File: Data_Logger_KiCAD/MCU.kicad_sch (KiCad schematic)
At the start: 47 parts, among them J1 USB_C_Receptacle_USB2.0_16P, J2 Screw_Terminal_01x02, J4 Conn_Coaxial_Small, J5 Conn_01x02, Q1 Q_NMOS_GSD, SW1 SW_Push, SW2 SW_Push, U2 ESP32-S3, Y2 Crystal, Y3 Crystal_GND24

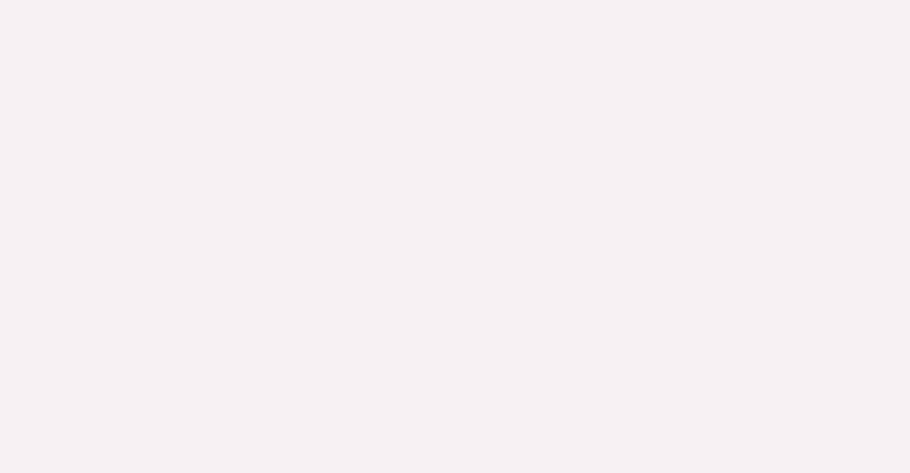
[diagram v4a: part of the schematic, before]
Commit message: update pcb from schem
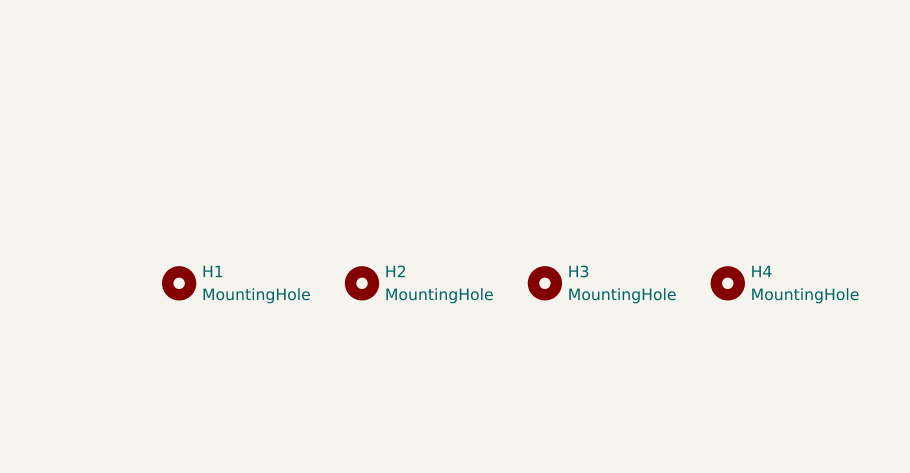
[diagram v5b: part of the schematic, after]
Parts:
- added H1, H2, H3, H4: MountingHole, MountingHole:MountingHole_2.2mm_M2, symbol Mechanical:MountingHole

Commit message: schematic recs
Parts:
- D4: value White -> Yellow
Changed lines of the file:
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@@
 			)
 		)
-		(property "Value" "White"
+		(property "Value" "Yellow"
 			(at 110.49 108.2674 90)
 			(effects

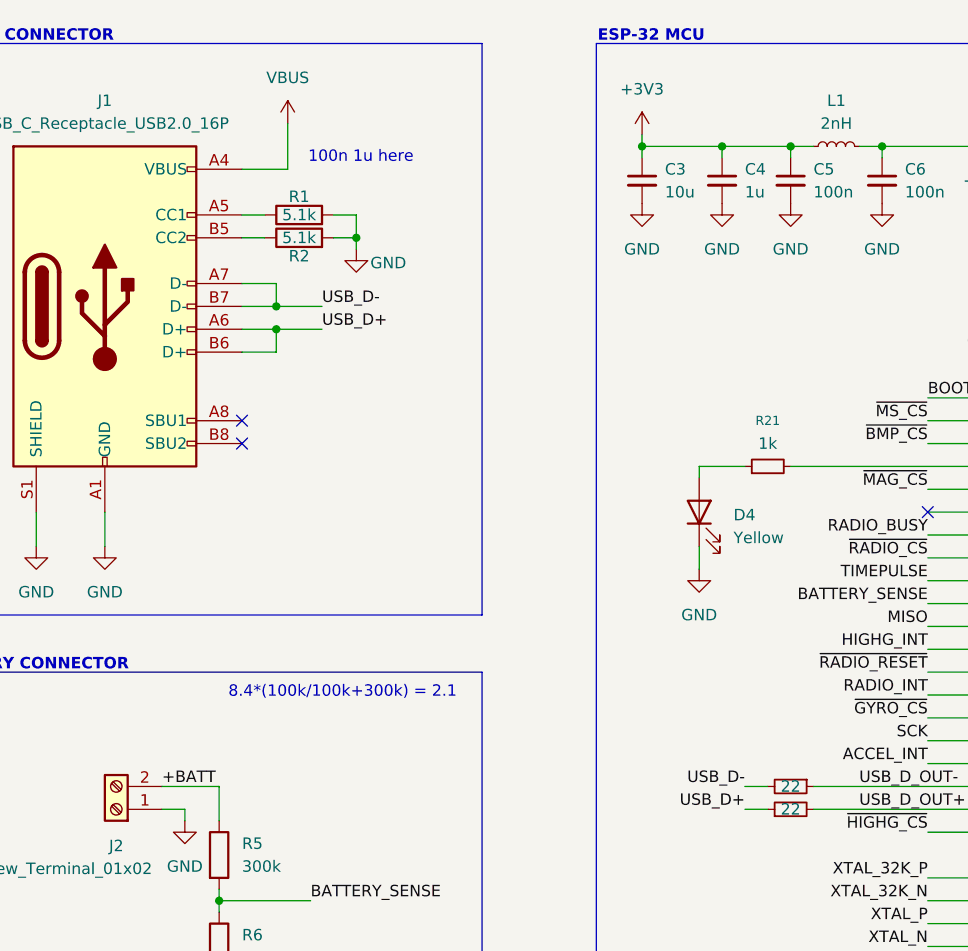
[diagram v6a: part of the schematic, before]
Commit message: fix battery sense + AIAA logo
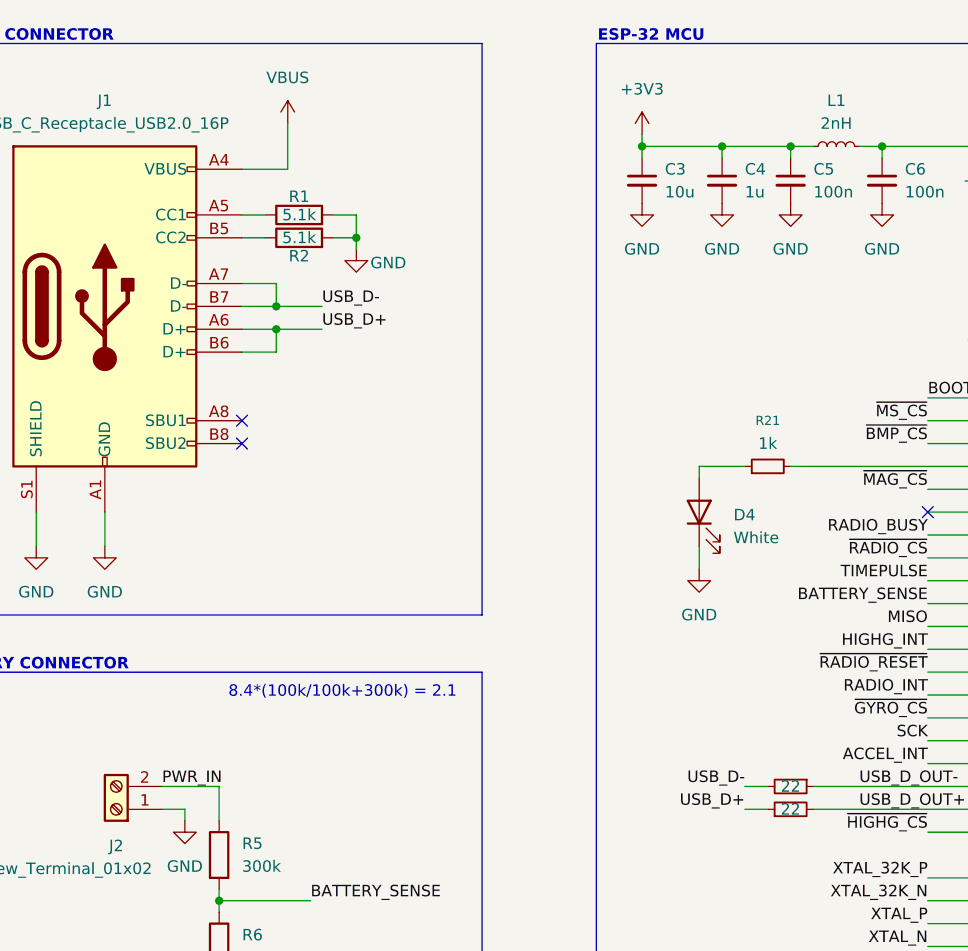
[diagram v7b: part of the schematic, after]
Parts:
- D4: value Yellow -> White
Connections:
- net +BATT: no longer J2.2 (Pin_2), R5.1
- net PWR_IN: now also J2.2 (Pin_2), R5.1
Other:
- note removed: "100n 1u here"
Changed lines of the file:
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@@
 		)
 	)
-	(text "100n 1u here"
-		(exclude_from_sim no)
-		(at 69.088 66.04 0)
-		(effects
-			(font
-				(size 1.27 1.27)
-			)
-		)
-	)
 	(text "BATTERY CONNECTOR\n"
 		(exclude_from_sim no)
@@
 		)
 	)
-	(label "+BATT"
+	(label "PWR_IN"
 		(at 46.99 135.89 0)
 		(effects
@@
 			)
 		)
-		(property "Value" "Yellow"
+		(property "Value" "White"
 			(at 110.49 108.2674 90)
 			(effects

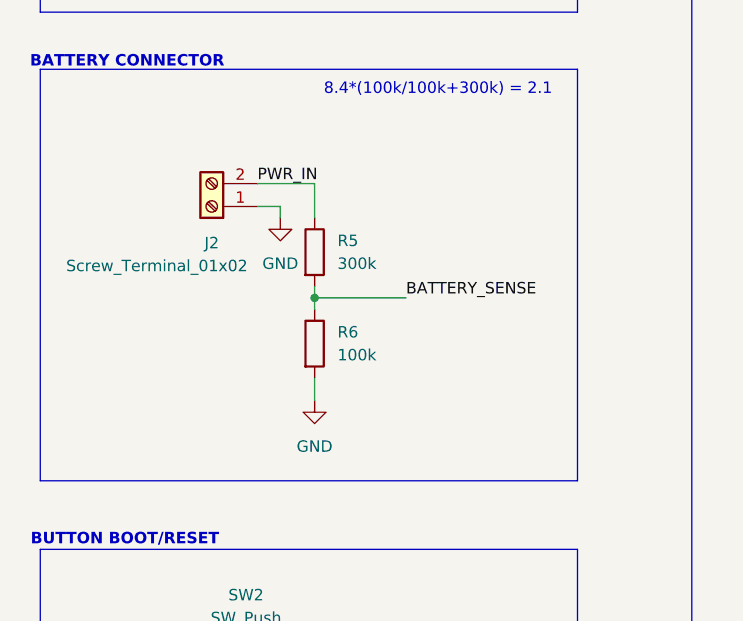
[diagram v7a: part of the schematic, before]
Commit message: add gnd vias below antenna
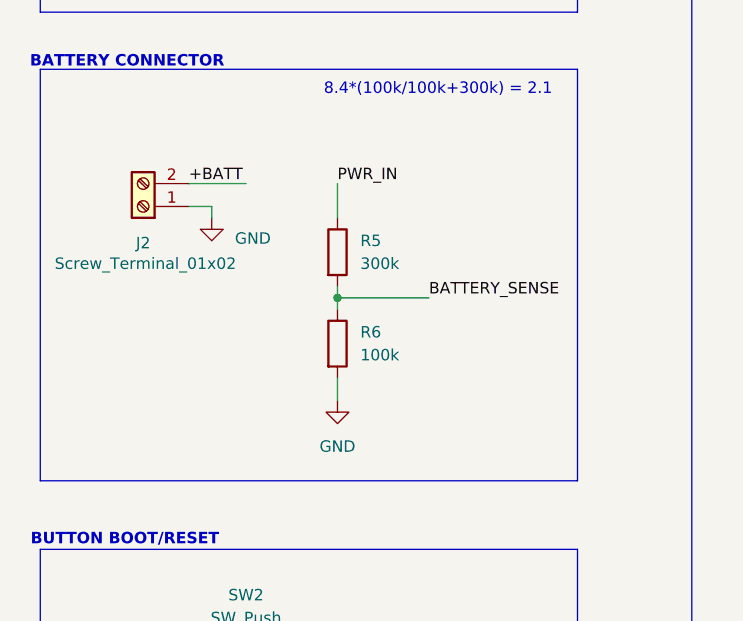
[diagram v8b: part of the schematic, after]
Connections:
- net +BATT: now also J2.2 (Pin_2)
- net PWR_IN: no longer J2.2 (Pin_2)
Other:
- moved on the sheet: J2, R5, R6
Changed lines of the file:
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@@
 	)
 	(junction
-		(at 53.34 148.59)
+		(at 55.88 148.59)
 		(diameter 0)
 		(color 0 0 0 0)
@@
 	(wire
 		(pts
-			(xy 46.99 135.89) (xy 53.34 135.89)
+			(xy 39.37 135.89) (xy 45.72 135.89)
 		)
 		(stroke
@@
 	(wire
 		(pts
-			(xy 46.99 138.43) (xy 49.53 138.43)
+			(xy 39.37 138.43) (xy 41.91 138.43)
 		)
 		(stroke
@@
 	(wire
 		(pts
-			(xy 53.34 148.59) (xy 53.34 149.86)
+			(xy 55.88 148.59) (xy 55.88 149.86)
 		)
 		(stroke
@@
 	(wire
 		(pts
-			(xy 53.34 147.32) (xy 53.34 148.59)
+			(xy 55.88 147.32) (xy 55.88 148.59)
 		)
 		(stroke
@@
 	(wire
 		(pts
-			(xy 53.34 157.48) (xy 53.34 160.02)
+			(xy 55.88 157.48) (xy 55.88 160.02)
 		)
 		(stroke
@@
 	(wire
 		(pts
+			(xy 55.88 135.89) (xy 55.88 139.7)
+		)
+		(stroke
+			(width 0)
+			(type default)
+		)
+	)
+	(wire
+		(pts
 			(xy 269.24 80.01) (xy 275.59 80.01)
 		)
@@
 	(wire
 		(pts
-			(xy 49.53 138.43) (xy 49.53 139.7)
+			(xy 41.91 138.43) (xy 41.91 139.7)
 		)
 		(stroke
@@
 	(wire
 		(pts
-			(xy 53.34 135.89) (xy 53.34 139.7)
-		)
-		(stroke
-			(width 0)
-			(type default)
-		)
-	)
-	(wire
-		(pts
 			(xy 148.59 74.93) (xy 148.59 76.2)
 		)
@@
 	(wire
 		(pts
-			(xy 53.34 148.59) (xy 63.5 148.59)
+			(xy 55.88 148.59) (xy 66.04 148.59)
 		)
 		(stroke
@@
 		)
 	)
-	(label "PWR_IN"
-		(at 46.99 135.89 0)
+	(label "+BATT"
+		(at 39.37 135.89 0)
 		(effects
 			(font
@@
 	)
 	(label "BATTERY_SENSE"
-		(at 63.5 148.59 0)
+		(at 66.04 148.59 0)
 		(effects
 			(font
@@
 		)
 	)
+	(label "PWR_IN"
+		(at 55.88 135.89 0)
+		(effects
+			(font
+				(size 1.27 1.27)
+			)
+			(justify left bottom)
+		)
+	)
 	(label "BATTERY_SENSE"
 		(at 132.08 115.57 180)
@@
 	(symbol
 		(lib_id "Connector:Screw_Terminal_01x02")
-		(at 41.91 138.43 180)
+		(at 34.29 138.43 180)
 		(unit 1)
 		(exclude_from_sim no)
@@
 		(dnp no)
 		(property "Reference" "J2"
-			(at 41.91 142.494 0)
+			(at 34.29 142.494 0)
 			(effects
 				(font
@@
 		)
 		(property "Value" "Screw_Terminal_01x02"
-			(at 35.814 145.034 0)
+			(at 34.544 144.78 0)
 			(effects
 				(font
@@
 		)
 		(property "Footprint" "TerminalBlock:TerminalBlock_Xinya_XY308-2.54-2P_1x02_P2.54mm_Horizontal"
-			(at 41.91 138.43 0)
+			(at 34.29 138.43 0)
 			(effects
 				(font
@@
 		)
 		(property "Datasheet" "~"
-			(at 41.91 138.43 0)
+			(at 34.29 138.43 0)
 			(effects
 				(font
@@
 		)
 		(property "Description" "Generic screw terminal, single row, 01x02, script generated (kicad-library-utils/schlib/autogen/connector/)"
-			(at 41.91 138.43 0)
+			(at 34.29 138.43 0)
 			(effects
 				(font
@@
 		)
 		(property "LCSC" ""
-			(at 41.91 138.43 0)
+			(at 34.29 138.43 0)
 			(effects
 				(font
@@
 	(symbol
 		(lib_id "Device:R")
-		(at 53.34 143.51 0)
+		(at 55.88 143.51 0)
 		(unit 1)
 		(exclude_from_sim no)
@@
 		(fields_autoplaced yes)
 		(property "Reference" "R5"
-			(at 55.88 142.2399 0)
+			(at 58.42 142.2399 0)
 			(effects
 				(font
@@
 		)
 		(property "Value" "300k"
-			(at 55.88 144.7799 0)
+			(at 58.42 144.7799 0)
 			(effects
 				(font
@@
 		)
 		(property "Footprint" "Resistor_SMD:R_0402_1005Metric"
-			(at 51.562 143.51 90)
+			(at 54.102 143.51 90)
 			(effects
 				(font
@@
 		)
 		(property "Datasheet" "~"
-			(at 53.34 143.51 0)
+			(at 55.88 143.51 0)
 			(effects
 				(font
@@
 		)
 		(property "Description" "Resistor"
-			(at 53.34 143.51 0)
+			(at 55.88 143.51 0)
 			(effects
 				(font
@@
 		)
 		(property "LCSC" "C25774"
-			(at 53.34 143.51 0)
+			(at 55.88 143.51 0)
 			(effects
 				(font
@@
 	(symbol
 		(lib_id "power:GND")
-		(at 49.53 139.7 0)
+		(at 41.91 139.7 0)
 		(unit 1)
 		(exclude_from_sim no)
@@
 		(on_board yes)
 		(dnp no)
-		(fields_autoplaced yes)
 		(property "Reference" "#PWR022"
-			(at 49.53 146.05 0)
+			(at 41.91 146.05 0)
 			(effects
 				(font
@@
 		)
 		(property "Value" "GND"
-			(at 49.53 144.78 0)
+			(at 46.482 141.986 0)
 			(effects
 				(font
@@
 		)
 		(property "Footprint" ""
-			(at 49.53 139.7 0)
+			(at 41.91 139.7 0)
 			(effects
 				(font
@@
 		)
 		(property "Datasheet" ""
-			(at 49.53 139.7 0)
+			(at 41.91 139.7 0)
 			(effects
 				(font
@@
 		)
 		(property "Description" "Power symbol creates a global label with name \"GND\" , ground"
-			(at 49.53 139.7 0)
+			(at 41.91 139.7 0)
 			(effects
 				(font
@@
 	(symbol
 		(lib_id "power:GND")
-		(at 53.34 160.02 0)
+		(at 55.88 160.02 0)
 		(unit 1)
 		(exclude_from_sim no)
@@
 		(fields_autoplaced yes)
 		(property "Reference" "#PWR024"
-			(at 53.34 166.37 0)
+			(at 55.88 166.37 0)
 			(effects
 				(font
@@
 		)
 		(property "Value" "GND"
-			(at 53.34 165.1 0)
+			(at 55.88 165.1 0)
 			(effects
 				(font
@@
 		)
 		(property "Footprint" ""
-			(at 53.34 160.02 0)
+			(at 55.88 160.02 0)
 			(effects
 				(font
@@
 		)
 		(property "Datasheet" ""
-			(at 53.34 160.02 0)
+			(at 55.88 160.02 0)
 			(effects
 				(font
@@
 		)
 		(property "Description" "Power symbol creates a global label with name \"GND\" , ground"
-			(at 53.34 160.02 0)
+			(at 55.88 160.02 0)
 			(effects
 				(font
@@
 	(symbol
 		(lib_id "Device:R")
-		(at 53.34 153.67 0)
+		(at 55.88 153.67 0)
 		(unit 1)
 		(exclude_from_sim no)
@@
 		(fields_autoplaced yes)
 		(property "Reference" "R6"
-			(at 55.88 152.3999 0)
+			(at 58.42 152.3999 0)
 			(effects
 				(font
@@
 		)
 		(property "Value" "100k"
-			(at 55.88 154.9399 0)
+			(at 58.42 154.9399 0)
 			(effects
 				(font
@@
 		)
 		(property "Footprint" "Resistor_SMD:R_0402_1005Metric"
-			(at 51.562 153.67 90)
+			(at 54.102 153.67 90)
 			(effects
 				(font
@@
 		)
 		(property "Datasheet" "~"
-			(at 53.34 153.67 0)
+			(at 55.88 153.67 0)
 			(effects
 				(font
@@
 		)
 		(property "Description" "Resistor"
-			(at 53.34 153.67 0)
+			(at 55.88 153.67 0)
 			(effects
 				(font
@@
 		)
 		(property "LCSC" "C25741"
-			(at 53.34 153.67 0)
+			(at 55.88 153.67 0)
 			(effects
 				(font
